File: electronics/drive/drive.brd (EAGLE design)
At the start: 35 x 25 mm, 11 parts, among them IC1 MEGA8-AI, IC2 MAX1483ESA, J1 AVR_SPI_PRG_6NS

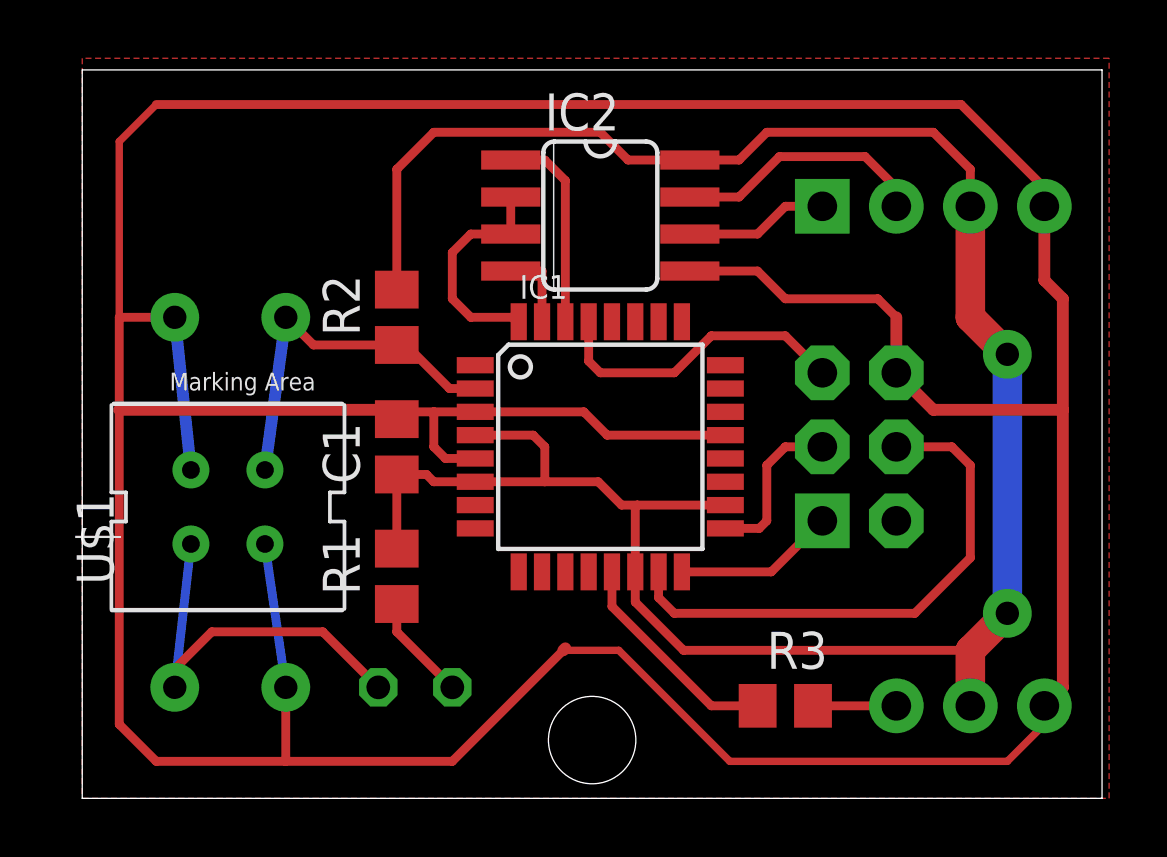
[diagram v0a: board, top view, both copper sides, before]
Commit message: Updating the board - More space for the programming connector - VCC connected to the programming connector - Removed the jumper wire
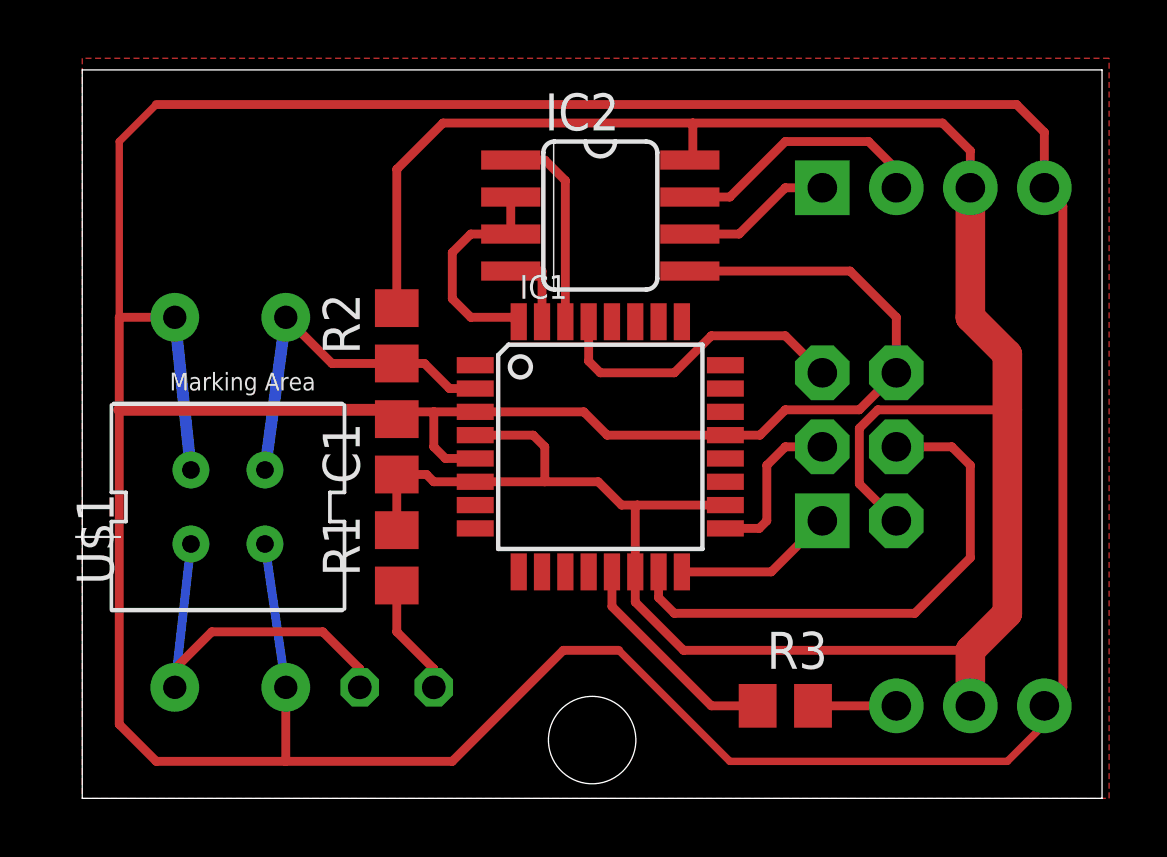
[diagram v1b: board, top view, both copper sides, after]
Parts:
- moved R2 0.64 mm to (10.8, 15.9)
- moved R1 0.64 mm to (10.8, 8.26)
- moved LED1 0.63 mm to (10.8, 3.81)
- moved JP1 0.63 mm to (25.4, 21.0)
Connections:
- net +5V: now also J1.2
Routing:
- net +5V: track 79.6 -> 90.5 mm, vias 2 -> 0
- net GND: track 163.4 -> 164.9 mm

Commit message: Updated value of the sensor resistor on a drive board.
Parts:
- R2: value 12k -> 33k
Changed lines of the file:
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@@
 </element>
 <element name="J1" library="SparkFun" package="2X3-NS" value="AVR_SPI_PRG_6NS" x="26.67" y="12.065" rot="MR90"/>
-<element name="R2" library="rcl" package="R0805" value="12k" x="10.795" y="15.875" rot="R90"/>
+<element name="R2" library="rcl" package="R0805" value="33k" x="10.795" y="15.875" rot="R90"/>
 <element name="R3" library="rcl" package="R0805" value="1k" x="24.13" y="3.175"/>
 </elements>
